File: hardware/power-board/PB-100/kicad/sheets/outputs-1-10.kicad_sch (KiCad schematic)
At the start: 0 parts

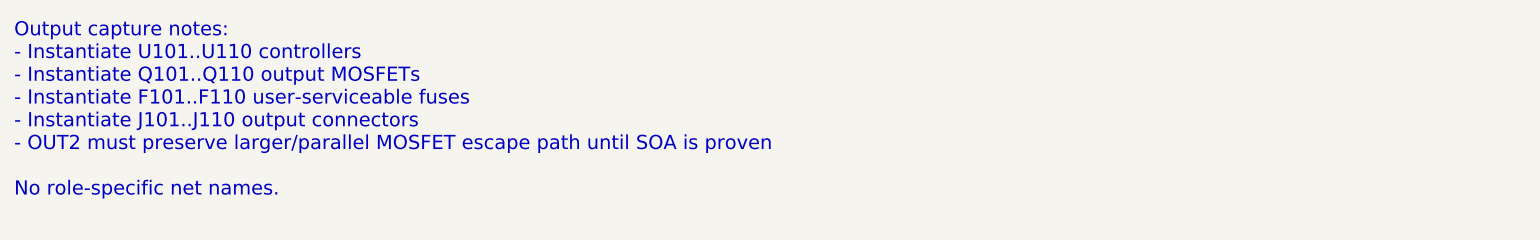
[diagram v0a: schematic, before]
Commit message: hardware: sync pb100 kicad sheet trace notes
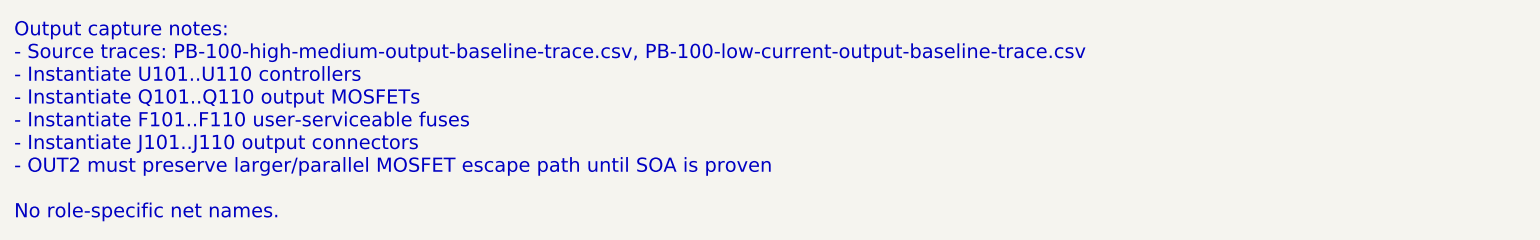
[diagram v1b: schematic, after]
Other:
- note added: "Output capture notes: - Source traces: PB-100-high-medium-output-baseline-trace.csv, PB-100-low-current-output-baseline-trace.csv - Instantiate U101..U110 controllers - Instantiate Q101..Q110 output MOSFETs - Instantiate F101..F110 user-serviceable fuses - Instantiate J101..J110 output connectors - OUT2 must preserve larger/parallel MOSFET escape path until SOA is proven No role-specific net name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"
- note removed: "Output capture notes: - Instantiate U101..U110 controllers - Instantiate Q101..Q110 output MOSFETs - Instantiate F101..F110 user-serviceable fuses - Instantiate J101..J110 output connectors - OUT2 must preserve larger/parallel MOSFET escape path until SOA is proven No role-specific net names."
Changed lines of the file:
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@@
     (comment 9 "Work queue: CAP-OUT-INST. Output instances capture follows output net expansion.")
     (comment 1 "Placeholder sheet. Instantiate OUT1 through OUT10 generic channels here.")
-    (comment 2 "Source: PB-100-schematic-instance-plan.csv.")
+    (comment 2 "Sources: PB-100-high-medium-output-baseline-trace.csv, PB-100-low-current-output-baseline-trace.csv, PB-100-schematic-instance-plan.csv.")
   )
-  (text "Output capture notes:\n- Instantiate U101..U110 controllers\n- Instantiate Q101..Q110 output MOSFETs\n- Instantiate F101..F110 user-serviceable fuses\n- Instantiate J101..J110 output connectors\n- OUT2 must preserve larger/parallel MOSFET escape path until SOA is proven\n\nNo role-specific net names."
+  (text "Output capture notes:\n- Source traces: PB-100-high-medium-output-baseline-trace.csv, PB-100-low-current-output-baseline-trace.csv\n- Instantiate U101..U110 controllers\n- Instantiate Q101..Q110 output MOSFETs\n- Instantiate F101..F110 user-serviceable fuses\n- Instantiate J101..J110 output connectors\n- OUT2 must preserve larger/parallel MOSFET escape path until SOA is proven\n\nNo role-specific net names."
     (at 25 30 0)
     (effects (font (size 2.0 2.0)) (justify left top))

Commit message: hardware: add pb100 output stage freeze reviews
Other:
- note added: "Output capture notes: - Source traces: PB-100-high-medium-output-baseline-trace.csv, PB-100-high-medium-output-freeze-review.csv, PB-100-low-current-output-baseline-trace.csv, PB-100-low-current-output-freeze-review.csv - Instantiate U101..U110 controllers - Instantiate Q101..Q110 output MOSFETs - Instantiate F101..F110 user-serviceable fuses - Instantiate J101..J110 output connectors - OUT2 must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"
- note removed: "Output capture notes: - Source traces: PB-100-high-medium-output-baseline-trace.csv, PB-100-low-current-output-baseline-trace.csv - Instantiate U101..U110 controllers - Instantiate Q101..Q110 output MOSFETs - Instantiate F101..F110 user-serviceable fuses - Instantiate J101..J110 output connectors - OUT2 must preserve larger/parallel MOSFET escape path until SOA is proven No role-specific net name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"
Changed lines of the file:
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@@
     (comment 9 "Work queue: CAP-OUT-INST. Output instances capture follows output net expansion.")
     (comment 1 "Placeholder sheet. Instantiate OUT1 through OUT10 generic channels here.")
-    (comment 2 "Sources: PB-100-high-medium-output-baseline-trace.csv, PB-100-low-current-output-baseline-trace.csv, PB-100-schematic-instance-plan.csv.")
+    (comment 2 "Sources: PB-100-high-medium-output-baseline-trace.csv, PB-100-high-medium-output-freeze-review.csv, PB-100-low-current-output-baseline-trace.csv, PB-100-low-current-output-freeze-review.csv, PB-100-schematic-instance-plan.csv.")
   )
-  (text "Output capture notes:\n- Source traces: PB-100-high-medium-output-baseline-trace.csv, PB-100-low-current-output-baseline-trace.csv\n- Instantiate U101..U110 controllers\n- Instantiate Q101..Q110 output MOSFETs\n- Instantiate F101..F110 user-serviceable fuses\n- Instantiate J101..J110 output connectors\n- OUT2 must preserve larger/parallel MOSFET escape path until SOA is proven\n\nNo role-specific net names."
+  (text "Output capture notes:\n- Source traces: PB-100-high-medium-output-baseline-trace.csv, PB-100-high-medium-output-freeze-review.csv, PB-100-low-current-output-baseline-trace.csv, PB-100-low-current-output-freeze-review.csv\n- Instantiate U101..U110 controllers\n- Instantiate Q101..Q110 output MOSFETs\n- Instantiate F101..F110 user-serviceable fuses\n- Instantiate J101..J110 output connectors\n- OUT2 must preserve larger/parallel MOSFET escape path until SOA is proven\n- OUT5/OUT8/OUT9 keep external-controller baseline and no direct 40 V smart-switch rail\n\nNo role-specific net names."
     (at 25 30 0)
     (effects (font (size 2.0 2.0)) (justify left top))

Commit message: Capture preliminary PB-100 schematic sheets
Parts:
- added F101, F102, F103, F104, F105, F106, F107, F108, F109, F110: OUTPUT_FUSE_CLASS_PRELIM, symbol PB100:PB100_OUTPUT_FUSE_CLASS_PRELIM
- added J101, J102, J103, J104, J105, J106, J107, J108, J109, J110: OUTPUT_CONNECTOR_CLASS_PRELIM, symbol PB100:PB100_OUTPUT_CONNECTOR_CLASS_PRELIM
- added Q101, Q102, Q103, Q104, Q105, Q106, Q107, Q108, Q109, Q110: SIDR626LDP_PRELIM, symbol PB100:PB100_SIDR626LDP_PRELIM
- added U101, U102, U103, U104, U105, U106, U107, U108, U109, U110: TPS48110AQDGXRQ1_PRELIM, symbol PB100:PB100_TPS48110AQDGXRQ1_PRELIM
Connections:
- new net GND: J101.2 (GND_RETURN), J102.2 (GND_RETURN), J103.2 (GND_RETURN), J104.2 (GND_RETURN), J105.2 (GND_RETURN), J106.2 (GND_RETURN), J107.2 (GND_RETURN), J108.2 (GND_RETURN), J109.2 (GND_RETURN), J110.2 (GND_RETURN), U101.6 (GND), U102.6 (GND), U103.6 (GND), U104.6 (GND), U105.6 (GND), U106.6 (GND), U107.6 (GND), U108.6 (GND), U109.6 (GND), U110.6 (GND)
- new net OUT10_BST: U110.12 (BST)
- new net OUT10_CS_N: U110.17 (CS-)
- new net OUT10_CS_P: U110.18 (CS+)
- new net OUT10_CTL: U110.1 (EN/UVLO)
- new net OUT10_DIODE: U110.10 (DIODE)
- new net OUT10_FLT: U110.4 (FLT_T), U110.5 (FLT_I)
- new net OUT10_FUSED: F110.2 (OUTn_FUSED), J110.1 (OUTn_LOAD)
- new net OUT10_GATE: Q110.4 (G), U110.15 (PU)
- new net OUT10_IMON: U110.7 (IMON)
- new net OUT10_ISCP_SET: U110.19 (ISCP)
- new net OUT10_IWRN_SET: U110.8 (IWRN)
- new net OUT10_OV_SET: U110.2 (OV)
- new net OUT10_PD: U110.14 (PD)
- new net OUT10_SRC: Q110.1 (S), Q110.2 (S), Q110.3 (S), U110.13 (SRC)
- new net OUT10_SWITCHED: F110.1 (OUTn_SWITCHED), Q110.5 (D), Q110.6 (D), Q110.7 (D), Q110.8 (D)
- new net OUT10_TMR: U110.9 (TMR)
- new net OUT1_BST: U101.12 (BST)
- new net OUT1_CS_N: U101.17 (CS-)
- new net OUT1_CS_P: U101.18 (CS+)
- new net OUT1_CTL: U101.1 (EN/UVLO)
- new net OUT1_DIODE: U101.10 (DIODE)
- new net OUT1_FLT: U101.4 (FLT_T), U101.5 (FLT_I)
- new net OUT1_FUSED: F101.2 (OUTn_FUSED), J101.1 (OUTn_LOAD)
- new net OUT1_GATE: Q101.4 (G), U101.15 (PU)
- new net OUT1_IMON: U101.7 (IMON)
- new net OUT1_ISCP_SET: U101.19 (ISCP)
- new net OUT1_IWRN_SET: U101.8 (IWRN)
- new net OUT1_OV_SET: U101.2 (OV)
- new net OUT1_PD: U101.14 (PD)
- new net OUT1_SRC: Q101.1 (S), Q101.2 (S), Q101.3 (S), U101.13 (SRC)
- new net OUT1_SWITCHED: F101.1 (OUTn_SWITCHED), Q101.5 (D), Q101.6 (D), Q101.7 (D), Q101.8 (D)
- new net OUT1_TMR: U101.9 (TMR)
- new net OUT2_BST: U102.12 (BST)
- new net OUT2_CS_N: U102.17 (CS-)
- new net OUT2_CS_P: U102.18 (CS+)
- new net OUT2_CTL: U102.1 (EN/UVLO)
- new net OUT2_DIODE: U102.10 (DIODE)
- new net OUT2_FLT: U102.4 (FLT_T), U102.5 (FLT_I)
- new net OUT2_FUSED: F102.2 (OUTn_FUSED), J102.1 (OUTn_LOAD)
- new net OUT2_GATE: Q102.4 (G), U102.15 (PU)
- new net OUT2_IMON: U102.7 (IMON)
- new net OUT2_ISCP_SET: U102.19 (ISCP)
- new net OUT2_IWRN_SET: U102.8 (IWRN)
- new net OUT2_OV_SET: U102.2 (OV)
- new net OUT2_PD: U102.14 (PD)
- new net OUT2_SRC: Q102.1 (S), Q102.2 (S), Q102.3 (S), U102.13 (SRC)
- new net OUT2_SWITCHED: F102.1 (OUTn_SWITCHED), Q102.5 (D), Q102.6 (D), Q102.7 (D), Q102.8 (D)
- new net OUT2_TMR: U102.9 (TMR)
- new net OUT3_BST: U103.12 (BST)
- new net OUT3_CS_N: U103.17 (CS-)
- new net OUT3_CS_P: U103.18 (CS+)
- new net OUT3_CTL: U103.1 (EN/UVLO)
- new net OUT3_DIODE: U103.10 (DIODE)
- new net OUT3_FLT: U103.4 (FLT_T), U103.5 (FLT_I)
- new net OUT3_FUSED: F103.2 (OUTn_FUSED), J103.1 (OUTn_LOAD)
- new net OUT3_GATE: Q103.4 (G), U103.15 (PU)
- new net OUT3_IMON: U103.7 (IMON)
- new net OUT3_ISCP_SET: U103.19 (ISCP)
- new net OUT3_IWRN_SET: U103.8 (IWRN)
- new net OUT3_OV_SET: U103.2 (OV)
- new net OUT3_PD: U103.14 (PD)
- new net OUT3_SRC: Q103.1 (S), Q103.2 (S), Q103.3 (S), U103.13 (SRC)
- new net OUT3_SWITCHED: F103.1 (OUTn_SWITCHED), Q103.5 (D), Q103.6 (D), Q103.7 (D), Q103.8 (D)
- new net OUT3_TMR: U103.9 (TMR)
- new net OUT4_BST: U104.12 (BST)
- new net OUT4_CS_N: U104.17 (CS-)
- new net OUT4_CS_P: U104.18 (CS+)
- new net OUT4_CTL: U104.1 (EN/UVLO)
- new net OUT4_DIODE: U104.10 (DIODE)
- new net OUT4_FLT: U104.4 (FLT_T), U104.5 (FLT_I)
- new net OUT4_FUSED: F104.2 (OUTn_FUSED), J104.1 (OUTn_LOAD)
- new net OUT4_GATE: Q104.4 (G), U104.15 (PU)
- new net OUT4_IMON: U104.7 (IMON)
- new net OUT4_ISCP_SET: U104.19 (ISCP)
- new net OUT4_IWRN_SET: U104.8 (IWRN)
- new net OUT4_OV_SET: U104.2 (OV)
- new net OUT4_PD: U104.14 (PD)
- new net OUT4_SRC: Q104.1 (S), Q104.2 (S), Q104.3 (S), U104.13 (SRC)
- new net OUT4_SWITCHED: F104.1 (OUTn_SWITCHED), Q104.5 (D), Q104.6 (D), Q104.7 (D), Q104.8 (D)
- new net OUT4_TMR: U104.9 (TMR)
- new net OUT5_BST: U105.12 (BST)
- new net OUT5_CS_N: U105.17 (CS-)
- new net OUT5_CS_P: U105.18 (CS+)
- new net OUT5_CTL: U105.1 (EN/UVLO)
- new net OUT5_DIODE: U105.10 (DIODE)
- new net OUT5_FLT: U105.4 (FLT_T), U105.5 (FLT_I)
- new net OUT5_FUSED: F105.2 (OUTn_FUSED), J105.1 (OUTn_LOAD)
- new net OUT5_GATE: Q105.4 (G), U105.15 (PU)
- new net OUT5_IMON: U105.7 (IMON)
- new net OUT5_ISCP_SET: U105.19 (ISCP)
- new net OUT5_IWRN_SET: U105.8 (IWRN)
- new net OUT5_OV_SET: U105.2 (OV)
- new net OUT5_PD: U105.14 (PD)
- new net OUT5_SRC: Q105.1 (S), Q105.2 (S), Q105.3 (S), U105.13 (SRC)
- new net OUT5_SWITCHED: F105.1 (OUTn_SWITCHED), Q105.5 (D), Q105.6 (D), Q105.7 (D), Q105.8 (D)
- new net OUT5_TMR: U105.9 (TMR)
- new net OUT6_BST: U106.12 (BST)
- new net OUT6_CS_N: U106.17 (CS-)
- new net OUT6_CS_P: U106.18 (CS+)
- new net OUT6_CTL: U106.1 (EN/UVLO)
- new net OUT6_DIODE: U106.10 (DIODE)
- new net OUT6_FLT: U106.4 (FLT_T), U106.5 (FLT_I)
- new net OUT6_FUSED: F106.2 (OUTn_FUSED), J106.1 (OUTn_LOAD)
- new net OUT6_GATE: Q106.4 (G), U106.15 (PU)
- new net OUT6_IMON: U106.7 (IMON)
- new net OUT6_ISCP_SET: U106.19 (ISCP)
- new net OUT6_IWRN_SET: U106.8 (IWRN)
- new net OUT6_OV_SET: U106.2 (OV)
- new net OUT6_PD: U106.14 (PD)
- new net OUT6_SRC: Q106.1 (S), Q106.2 (S), Q106.3 (S), U106.13 (SRC)
- new net OUT6_SWITCHED: F106.1 (OUTn_SWITCHED), Q106.5 (D), Q106.6 (D), Q106.7 (D), Q106.8 (D)
- new net OUT6_TMR: U106.9 (TMR)
- new net OUT7_BST: U107.12 (BST)
- new net OUT7_CS_N: U107.17 (CS-)
- new net OUT7_CS_P: U107.18 (CS+)
- new net OUT7_CTL: U107.1 (EN/UVLO)
- new net OUT7_DIODE: U107.10 (DIODE)
- new net OUT7_FLT: U107.4 (FLT_T), U107.5 (FLT_I)
- new net OUT7_FUSED: F107.2 (OUTn_FUSED), J107.1 (OUTn_LOAD)
- new net OUT7_GATE: Q107.4 (G), U107.15 (PU)
- new net OUT7_IMON: U107.7 (IMON)
- new net OUT7_ISCP_SET: U107.19 (ISCP)
- new net OUT7_IWRN_SET: U107.8 (IWRN)
- new net OUT7_OV_SET: U107.2 (OV)
- new net OUT7_PD: U107.14 (PD)
- new net OUT7_SRC: Q107.1 (S), Q107.2 (S), Q107.3 (S), U107.13 (SRC)
- new net OUT7_SWITCHED: F107.1 (OUTn_SWITCHED), Q107.5 (D), Q107.6 (D), Q107.7 (D), Q107.8 (D)
- new net OUT7_TMR: U107.9 (TMR)
- new net OUT8_BST: U108.12 (BST)
- new net OUT8_CS_N: U108.17 (CS-)
- new net OUT8_CS_P: U108.18 (CS+)
- new net OUT8_CTL: U108.1 (EN/UVLO)
- new net OUT8_DIODE: U108.10 (DIODE)
- new net OUT8_FLT: U108.4 (FLT_T), U108.5 (FLT_I)
- new net OUT8_FUSED: F108.2 (OUTn_FUSED), J108.1 (OUTn_LOAD)
- new net OUT8_GATE: Q108.4 (G), U108.15 (PU)
- new net OUT8_IMON: U108.7 (IMON)
- new net OUT8_ISCP_SET: U108.19 (ISCP)
- new net OUT8_IWRN_SET: U108.8 (IWRN)
- new net OUT8_OV_SET: U108.2 (OV)
- new net OUT8_PD: U108.14 (PD)
- new net OUT8_SRC: Q108.1 (S), Q108.2 (S), Q108.3 (S), U108.13 (SRC)
- new net OUT8_SWITCHED: F108.1 (OUTn_SWITCHED), Q108.5 (D), Q108.6 (D), Q108.7 (D), Q108.8 (D)
- new net OUT8_TMR: U108.9 (TMR)
- new net OUT9_BST: U109.12 (BST)
- new net OUT9_CS_N: U109.17 (CS-)
- new net OUT9_CS_P: U109.18 (CS+)
- new net OUT9_CTL: U109.1 (EN/UVLO)
- new net OUT9_DIODE: U109.10 (DIODE)
- new net OUT9_FLT: U109.4 (FLT_T), U109.5 (FLT_I)
- new net OUT9_FUSED: F109.2 (OUTn_FUSED), J109.1 (OUTn_LOAD)
- new net OUT9_GATE: Q109.4 (G), U109.15 (PU)
- new net OUT9_IMON: U109.7 (IMON)
- new net OUT9_ISCP_SET: U109.19 (ISCP)
- new net OUT9_IWRN_SET: U109.8 (IWRN)
- new net OUT9_OV_SET: U109.2 (OV)
- new net OUT9_PD: U109.14 (PD)
- new net OUT9_SRC: Q109.1 (S), Q109.2 (S), Q109.3 (S), U109.13 (SRC)
- new net OUT9_SWITCHED: F109.1 (OUTn_SWITCHED), Q109.5 (D), Q109.6 (D), Q109.7 (D), Q109.8 (D)
- new net OUT9_TMR: U109.9 (TMR)
- new net VBAT_PROT: U101.20 (VS), U101.3 (INP), U102.20 (VS), U102.3 (INP), U103.20 (VS), U103.3 (INP), U104.20 (VS), U104.3 (INP), U105.20 (VS), U105.3 (INP), U106.20 (VS), U106.3 (INP), U107.20 (VS), U107.3 (INP), U108.20 (VS), U108.3 (INP), U109.20 (VS), U109.3 (INP), U110.20 (VS), U110.3 (INP)
- no-connect marks 0 -> 10
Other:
- note added: "Outputs capture notes: - Source traces: PB-100-high-medium-output-baseline-trace.csv, PB-100-high-medium-output-freeze-review.csv, PB-100-low-current-output-baseline-trace.csv, PB-100-low-current-output-freeze-review.csv - OUT1 through OUT10 remain generic hardware channels - OUT2 SOA and per-class values remain schematic-freeze blockers No PCB layout from this preliminary capture."
- note removed: "Output capture notes: - Source traces: PB-100-high-medium-output-baseline-trace.csv, PB-100-high-medium-output-freeze-review.csv, PB-100-low-current-output-baseline-trace.csv, PB-100-low-current-output-freeze-review.csv - Instantiate U101..U110 controllers - Instantiate Q101..Q110 output MOSFETs - Instantiate F101..F110 user-serviceable fuses - Instantiate J101..J110 output connectors - OUT2 must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"
